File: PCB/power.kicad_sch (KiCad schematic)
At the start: 39 parts, among them Q1 STT6N3LLH6_C3021100, Q3 BSS138, U13 INA226, U14 TPS26630RGE, U6 MP8859GQ-0000-Z

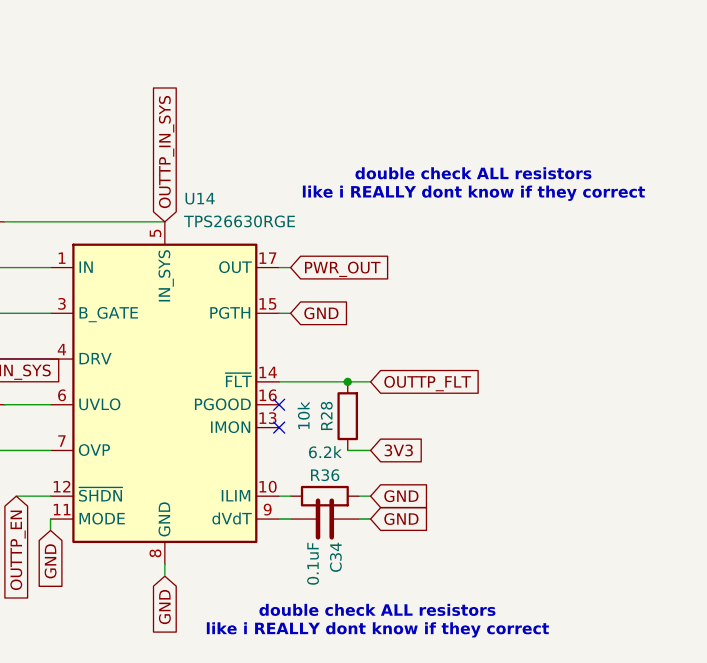
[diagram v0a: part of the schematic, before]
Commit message: Fix MPN number, adjust footprint, production files
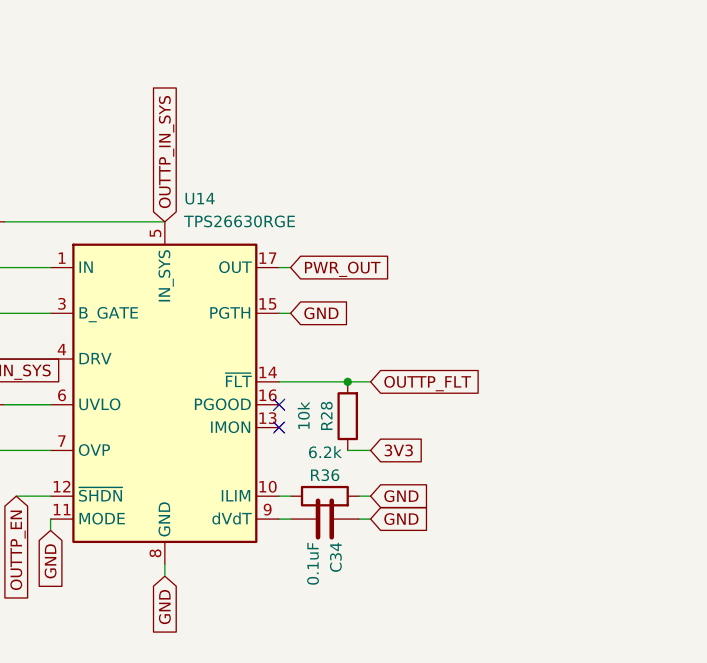
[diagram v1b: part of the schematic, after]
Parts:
- R53: footprint Resistor_SMD:R_0603_1608Metric -> Resistor_SMD:R_0402_1005Metric
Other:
- note removed: "double check ALL resistors like i REALLY dont know if they correct"
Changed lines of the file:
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@@
 	(generator_version "10.0")
 	(paper "A4")
-	(text "double check ALL resistors\nlike i REALLY dont know if they correct\n"
-		(exclude_from_sim no)
-		(at 252.73 103.886 0)
-		(effects
-			(font
-				(size 1.27 1.27)
-				(thickness 0.254)
-				(bold yes)
-			)
-		)
-	)
-	(text "double check ALL resistors\nlike i REALLY dont know if they correct\n"
-		(exclude_from_sim no)
-		(at 242.062 152.4 0)
-		(effects
-			(font
-				(size 1.27 1.27)
-				(thickness 0.254)
-				(bold yes)
-			)
-		)
-	)
 	(junction
 		(at 171.45 77.47)
@@
 			)
 		)
-		(property "Footprint" "Resistor_SMD:R_0603_1608Metric"
+		(property "Footprint" "Resistor_SMD:R_0402_1005Metric"
 			(at 196.85 126.492 90)
 			(hide yes)

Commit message: Add BOM and screenshots and cleanup. Updated PCB for fixed footprint for capacitor.
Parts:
- C10: footprint Capacitor_SMD:C_0402_1005Metric -> Capacitor_SMD:C_0805_2012Metric; MPN CGA2B2X7R1E223KT0Y0F -> CL21A226MAQNNNE
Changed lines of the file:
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@@
 			)
 		)
-		(property "Footprint" "Capacitor_SMD:C_0402_1005Metric"
+		(property "Footprint" "Capacitor_SMD:C_0805_2012Metric"
 			(at 59.9948 58.42 0)
 			(hide yes)
@@
 			)
 		)
-		(property "MPN" "CGA2B2X7R1E223KT0Y0F"
+		(property "MPN" "CL21A226MAQNNNE"
 			(at 60.96 62.23 0)
 			(hide yes)
